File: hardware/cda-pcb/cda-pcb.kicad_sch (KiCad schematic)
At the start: 187 parts, among them J1 ICD15S13E4GX00LF, J2 ICD15S13E4GX00LF, J3 ICD15S13E4GX00LF, J4 ICD15S13E4GX00LF, J6 Conn_01x06, P1 0022272021, U1 ADS124S08IRHBT, U10 SN74AHCT125RGYR, U2 ADS124S08IRHBT, U3 ADS124S08IRHBT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

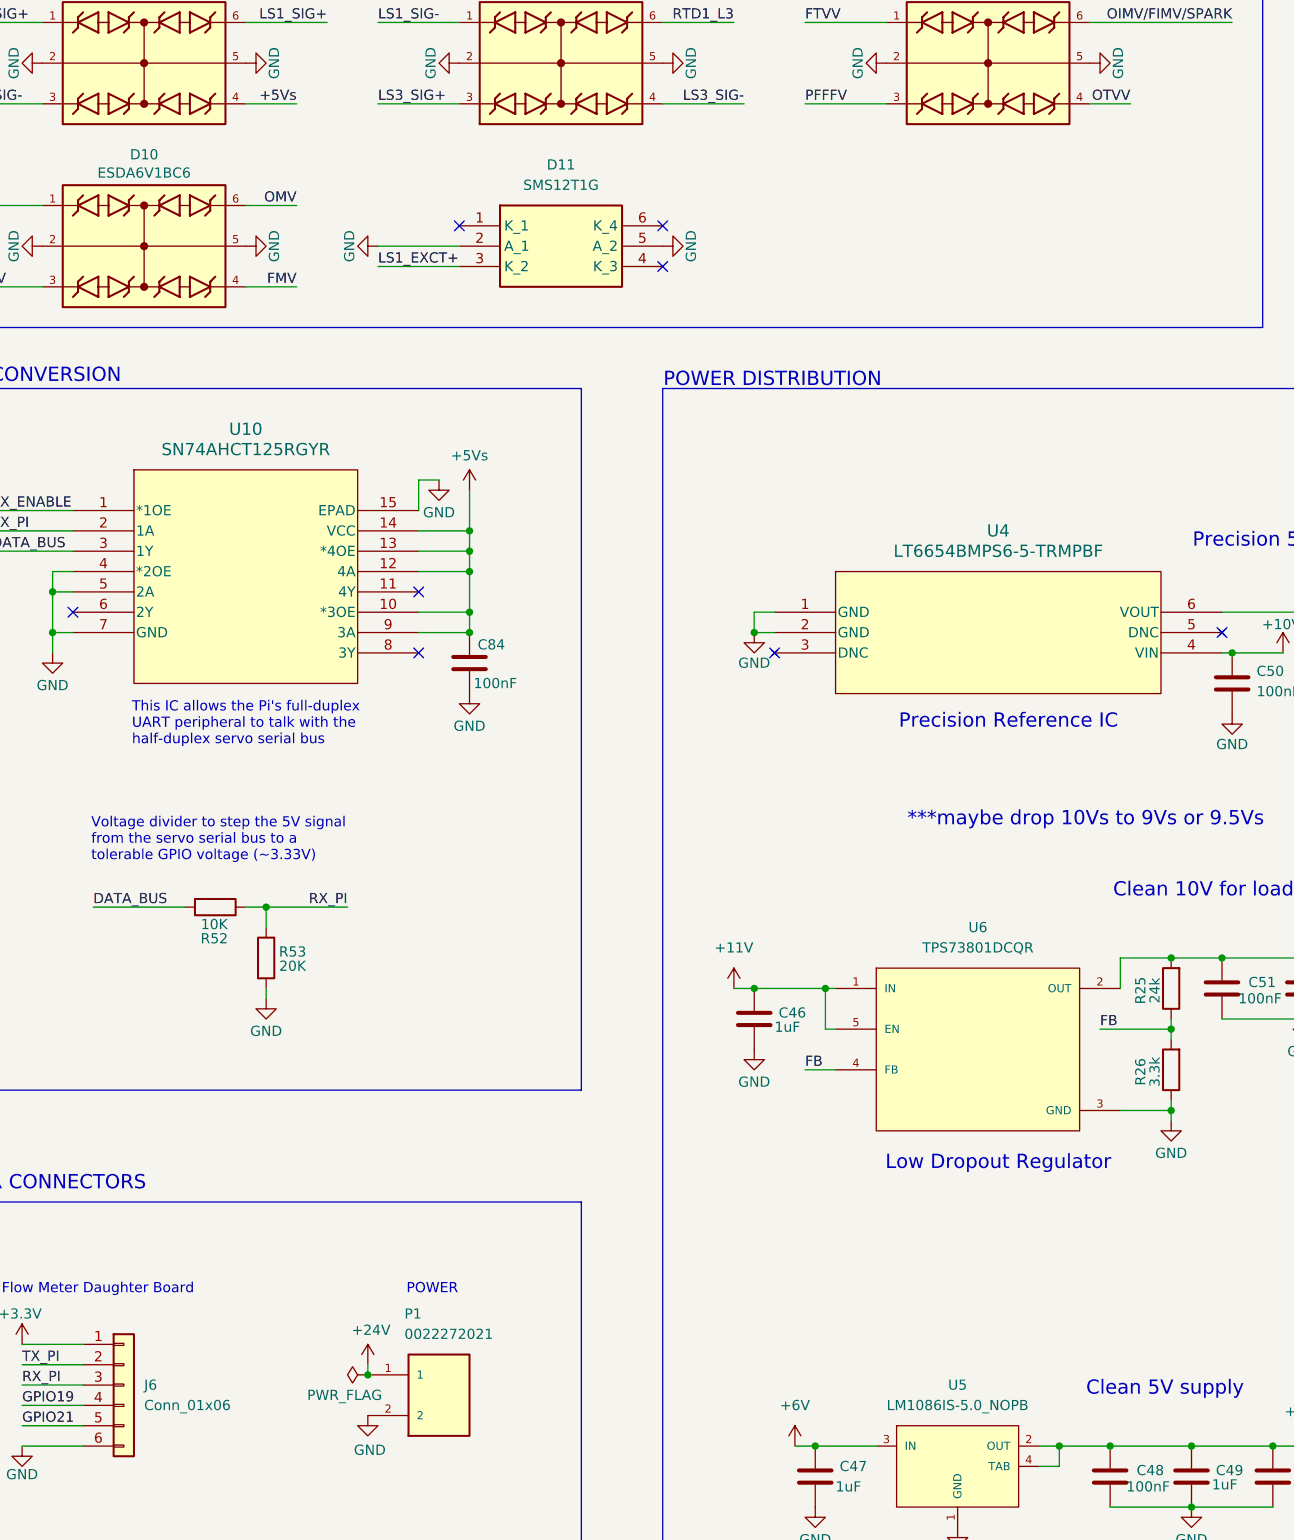
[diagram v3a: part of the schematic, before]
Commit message: added ESD protection to daughterboard & fiducials
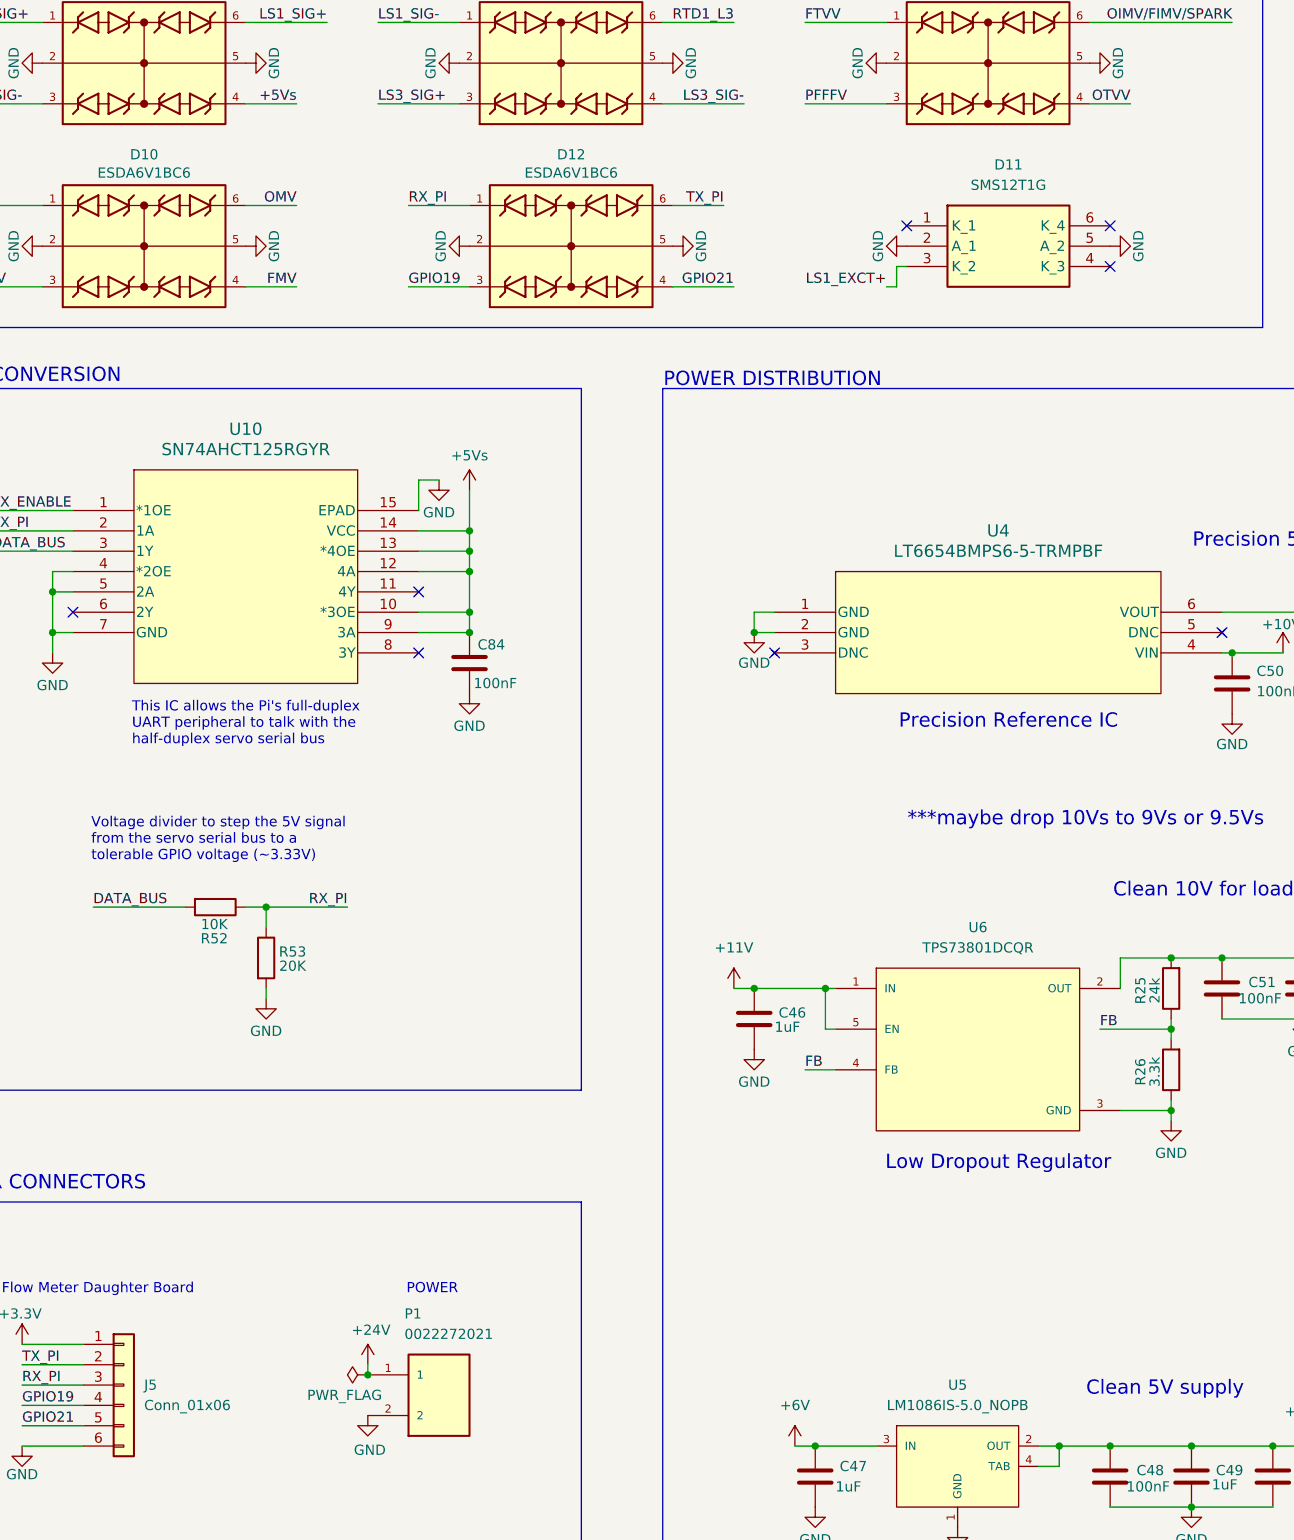
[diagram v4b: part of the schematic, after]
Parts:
- added D12: ESDA6V1BC6, ESDA6V1BC6:SOT95P280X145-6N, symbol ESDA6V1BC6:ESDA6V1BC6
- renumbered J6 to J5
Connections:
- net GND: now also D12.2, D12.5
- net GPIO19: now also D12.3
- net GPIO21: now also D12.4
- net RX_PI: now also D12.1
- net TX_PI: now also D12.6
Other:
- moved on the sheet: D11

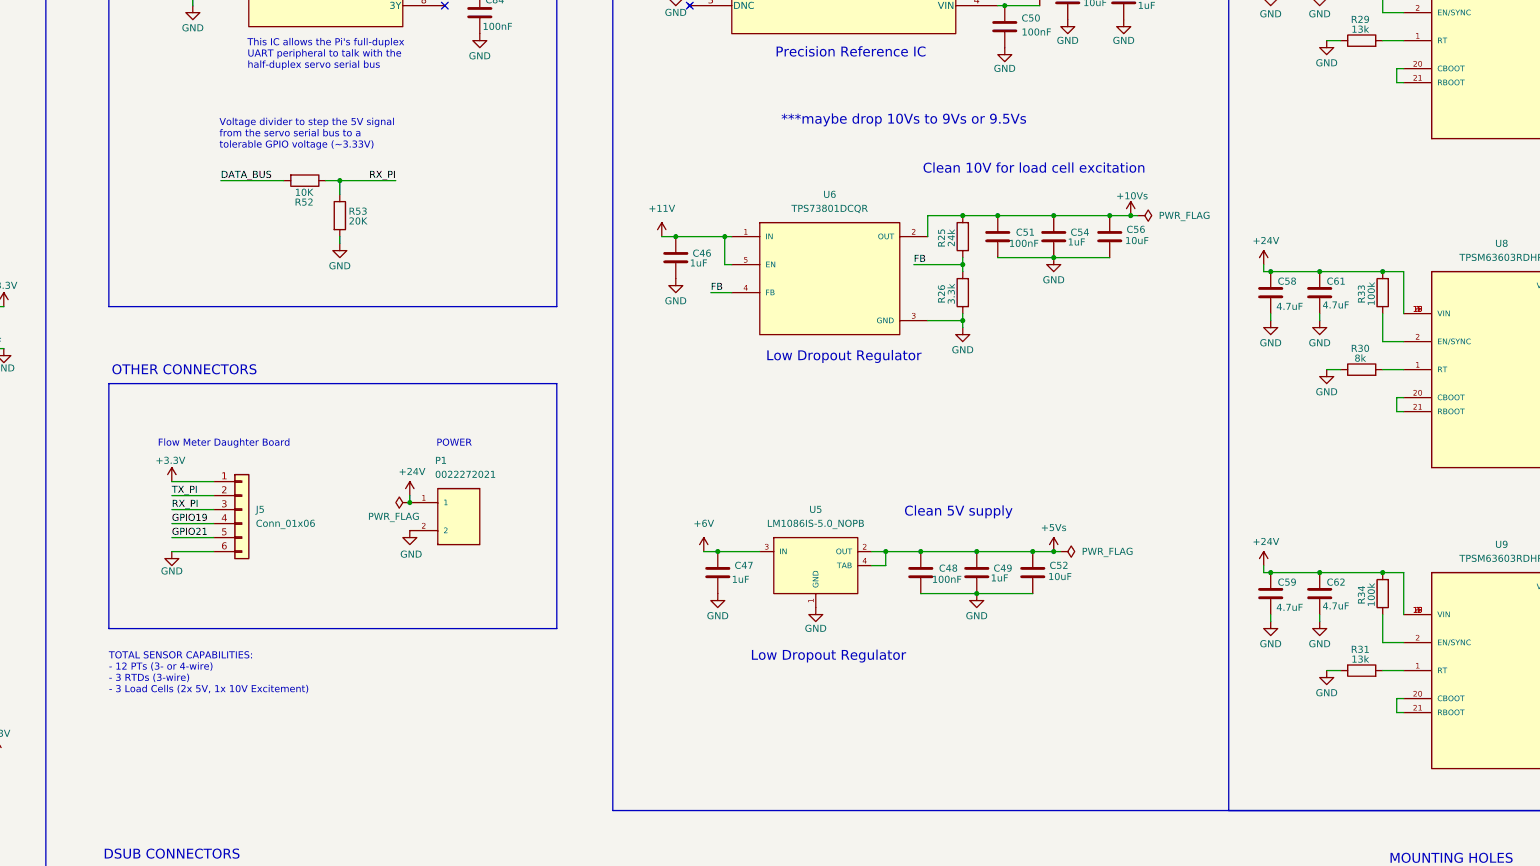
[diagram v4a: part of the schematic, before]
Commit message: add fiducials, remove handsoldered footprints, added indicator LEDs
Add board backups and make multiple PCB/schematic edits: adjust fiducial positions, add a new via, and tweak component and label coordinates for alignment. Add several schematic symbols and instances (LEDs, +5V/+9V/+10V power symbols, resistors R49/R63) and numerous small wire segments to connect indicators. Update footprints for several capacitors/inductors/ICs and simplify some footprint names. Also change KiCad project preference (high_contrast_mode) and apply general cleanup/positioning adjustments across cda-pcb.kicad_pcb and cda-pcb.kicad_sch.
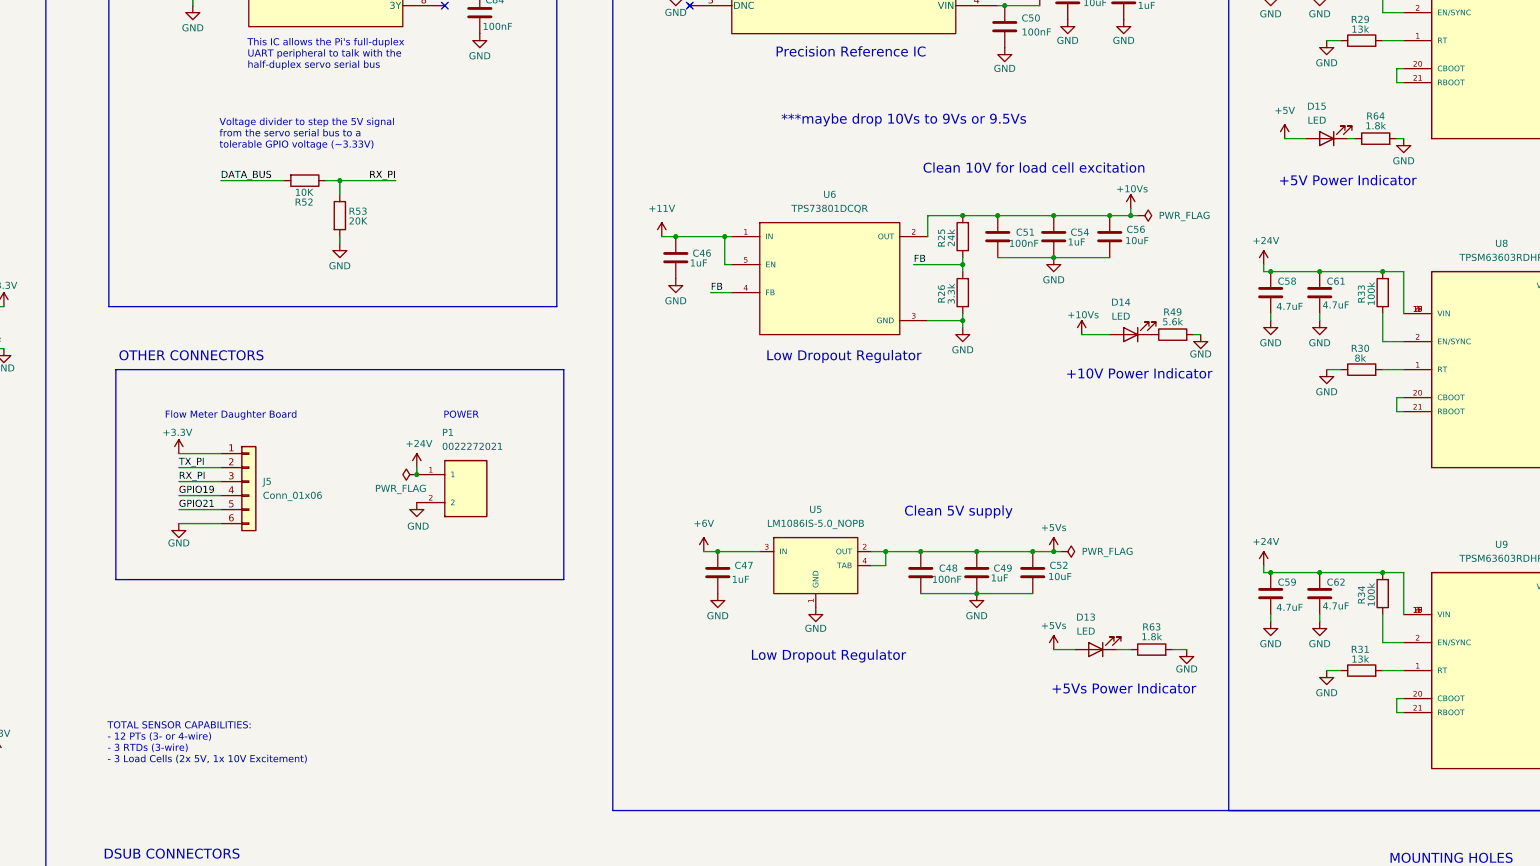
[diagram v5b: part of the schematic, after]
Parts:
- added D13, D14, D15: LED, LED_SMD:LED_0805_2012Metric, symbol Device:LED
- added R49: 5.6k, Resistor_SMD:R_0603_1608Metric, symbol Device:R
- added R63, R64: 1.8k, Resistor_SMD:R_0603_1608Metric, symbol Device:R
- C10, C11, C12, C13, C7, C8, C85, C86, C9: footprint Capacitor_SMD:C_0603_1608Metric_Pad1.08x0.95mm_HandSolder -> Capacitor_SMD:C_0603_1608Metric
- C57, C58, C59, C60, C61, C62: footprint Capacitor_SMD:C_0805_2012Metric_Pad1.18x1.45mm_HandSolder -> Capacitor_SMD:C_0805_2012Metric
- C63, C64, C65, C69, C70, C71: footprint Inductor_SMD:L_1206_3216Metric_Pad1.42x1.75mm_HandSolder -> Capacitor_SMD:C_1206_3216Metric
- U3: footprint footprintsADC:RHB0032M -> ADS124S08IRHBT:QFN50P500X500X100-33N
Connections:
- net +10Vs: now also D14.2 (A)
- net +5V: now also D15.2 (A)
- net +5Vs: now also D13.2 (A)
- net GND: now also R49.2, R63.2, R64.2
- new net: D14.1 (K), R49.1
- new net: D15.1 (K), R64.1
- new net: D13.1 (K), R63.1
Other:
- note added: "+10V Power Indicator"
- note added: "+5V Power Indicator"
- note added: "+5Vs Power Indicator"
- moved on the sheet: J5, P1

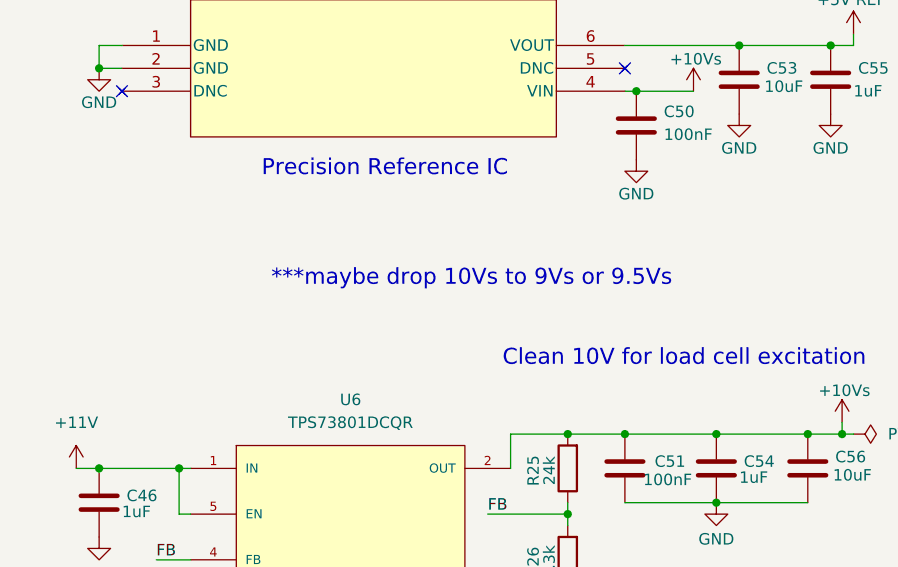
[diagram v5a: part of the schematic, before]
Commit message: addfed stitching vias
Modify PCB to add numerous free vias (mostly on net 2/GND) and refresh UUIDs for multiple pads/power pins. Updated cda-pcb.kicad_pcb with many new via entries and coordinate adjustments; supporting KiCad files (cda-pcb.kicad_prl, cda-pcb.kicad_sch, fp-info-cache) were also updated. Several old backup ZIPs under hardware/cda-pcb/cda-pcb-backups were removed and new timestamped backups were added.
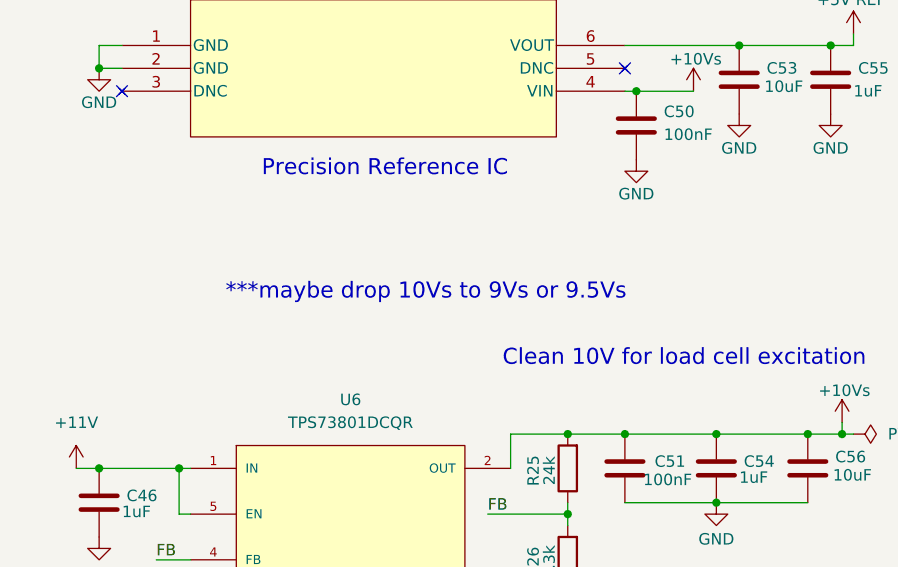
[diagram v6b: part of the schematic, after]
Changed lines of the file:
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@@
 	(text "***maybe drop 10Vs to 9Vs or 9.5Vs"
 		(exclude_from_sim no)
-		(at 397.002 189.738 0)
+		(at 391.922 191.262 0)
 		(effects
 			(font
